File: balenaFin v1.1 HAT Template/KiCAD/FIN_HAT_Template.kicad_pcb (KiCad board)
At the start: 2 copper layers, 90 x 73 mm, 6 parts, among them J2 Conn_02x02_Top_Bottom, J3 Conn_02x09_Top_Bottom, J4 Conn_01x04_Female

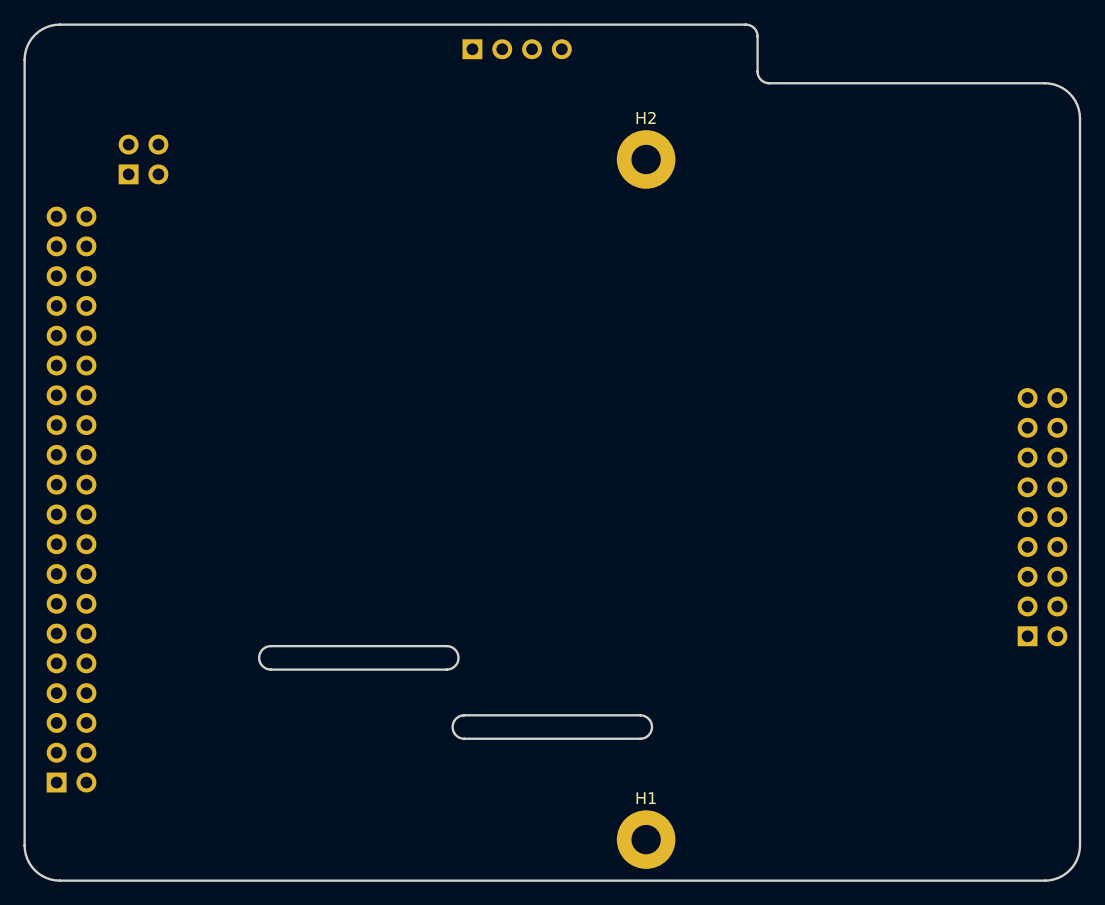
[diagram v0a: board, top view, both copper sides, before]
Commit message: Created a lib for our schematic symbols
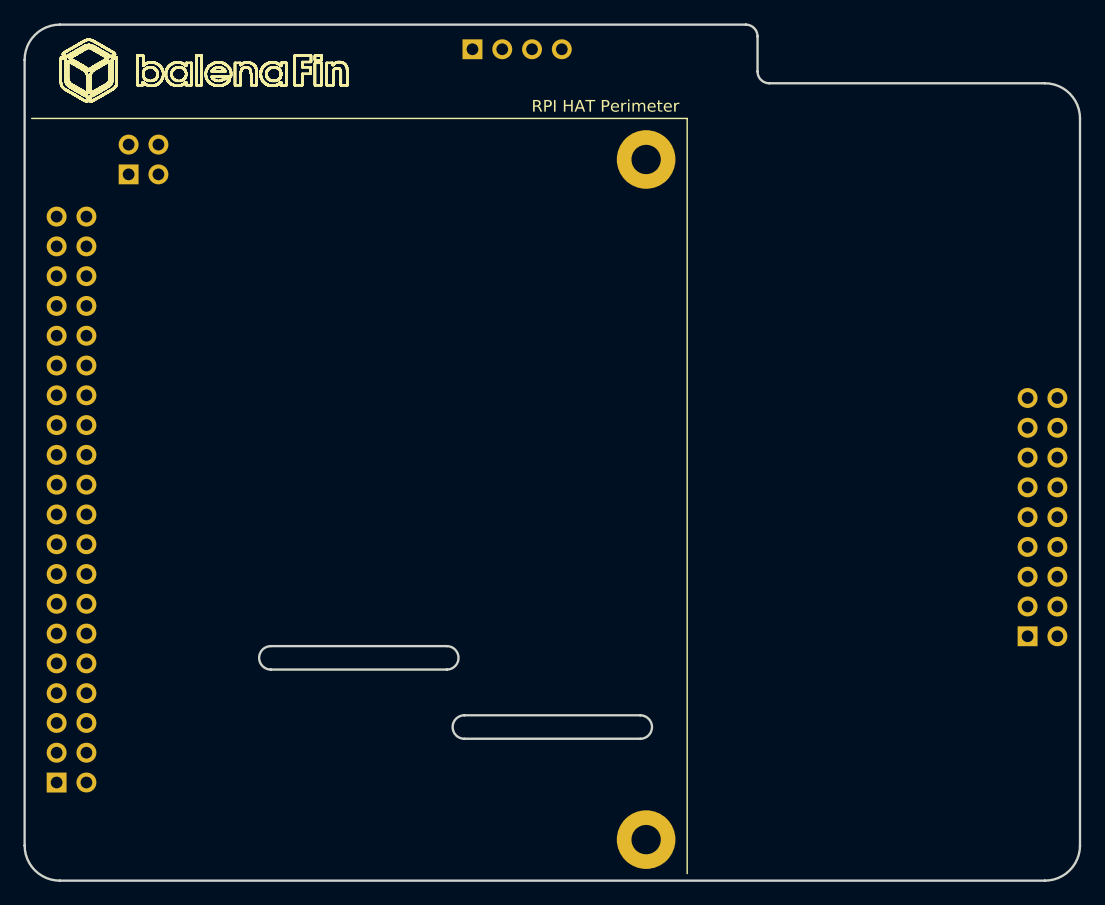
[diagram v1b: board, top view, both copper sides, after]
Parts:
- removed Je: Raspberry_Pi_2_3, Connector_PinHeader_2.54mm:PinHeader_2x20_P2.54mm_Vertical
- added J1: Raspberry_Pi_2_3, Connector_PinHeader_2.54mm:PinHeader_2x20_P2.54mm_Vertical, B.Cu at (105.6, 125.0)
- J2: value Conn_02x02_Top_Bottom -> POE_Header
- J3: value Conn_02x09_Top_Bottom -> Co-Processor_Header
- J4: value Conn_01x04_Female -> USB_Header
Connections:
- J3 pad 17: Net-(J3-Pad17) -> GND
- J4 pad 1: Net-(J4-Pad1) -> +5V
- J4 pad 4: Net-(J4-Pad4) -> GND
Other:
- board text added: "RPI HAT Perimeter"

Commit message: Created footrpints lib - Fixed the mirrored footprints issue - Added the dimenions
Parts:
- J1: footprint Connector_PinHeader_2.54mm:PinHeader_2x20_P2.54mm_Vertical -> FIN HAT Template:PinHeader_2x20_P2.54mm_Vertical
- J2: footprint Connector_PinHeader_2.54mm:PinHeader_2x02_P2.54mm_Vertical -> FIN HAT Template:PinHeader_2x02_P2.54mm_Vertical
- J3: footprint Connector_PinHeader_2.54mm:PinHeader_2x09_P2.54mm_Vertical -> FIN HAT Template:PinHeader_2x09_P2.54mm_Vertical
- J4: footprint Connector_PinHeader_2.54mm:PinHeader_1x04_P2.54mm_Vertical -> FIN HAT Template:PinHeader_1x04_P2.54mm_Vertical
- moved J1 24.2 mm to (106.9, 100.8)
- moved J3 10.2 mm to (189.7, 102.3)
- moved J4 3.81 mm to (144.9, 62.5)
- moved J2 1.80 mm to (113.0, 71.8)
